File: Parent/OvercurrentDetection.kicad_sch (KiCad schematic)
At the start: 2 parts, among them U62 INA138

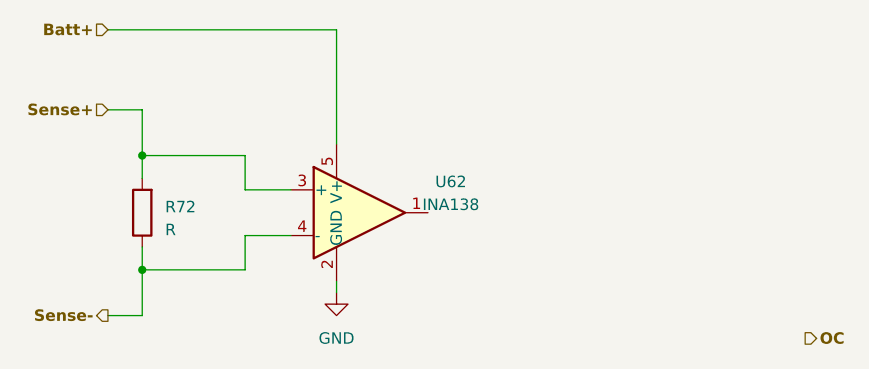
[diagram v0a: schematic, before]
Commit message: Updated Parent - Moved workspace to cloud
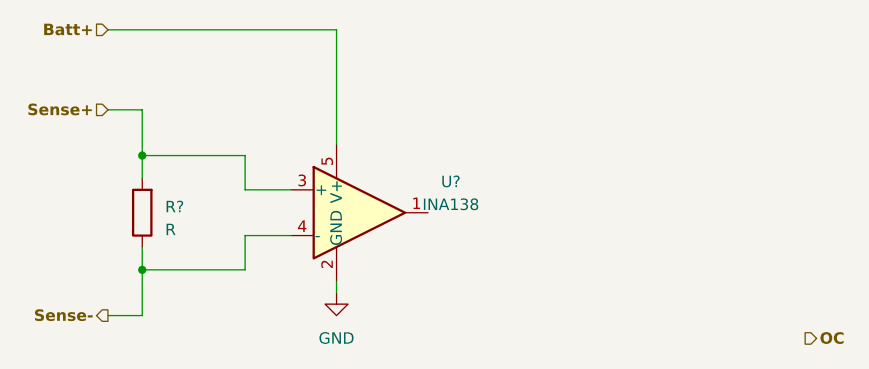
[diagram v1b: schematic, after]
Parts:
- renumbered R72 to R?, U62 to U?
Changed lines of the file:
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@@
   (symbol (lib_id "Amplifier_Current:INA138") (at 149.86 85.09 0) (unit 1)
     (in_bom yes) (on_board yes) (dnp no) (fields_autoplaced)
-    (property "Reference" "U62" (at 160.02 81.6611 0)
+    (property "Reference" "U?" (at 160.02 81.6611 0)
       (effects (font (size 1.27 1.27)))
     )
@@
       (project "Parent"
         (path "/1451ec1d-c665-471b-ba41-1d89ef6a63bf/687e81f5-5c64-42d1-9826-1f675bc9cd55"
-          (reference "U62") (unit 1)
+          (reference "U?") (unit 1)
         )
       )
@@
   (symbol (lib_id "power:GND") (at 147.32 93.98 0) (unit 1)
     (in_bom yes) (on_board yes) (dnp no) (fields_autoplaced)
-    (property "Reference" "#PWR029" (at 147.32 100.33 0)
+    (property "Reference" "#PWR?" (at 147.32 100.33 0)
       (effects (font (size 1.27 1.27)) hide)
     )
@@
       (project "Parent"
         (path "/1451ec1d-c665-471b-ba41-1d89ef6a63bf/687e81f5-5c64-42d1-9826-1f675bc9cd55"
-          (reference "#PWR029") (unit 1)
+          (reference "#PWR?") (unit 1)
         )
       )
@@
   (symbol (lib_id "Device:R") (at 125.73 85.09 180) (unit 1)
     (in_bom yes) (on_board yes) (dnp no) (fields_autoplaced)
-    (property "Reference" "R72" (at 128.27 84.455 0)
+    (property "Reference" "R?" (at 128.27 84.455 0)
       (effects (font (size 1.27 1.27)) (justify right))
     )
@@
       (project "Parent"
         (path "/1451ec1d-c665-471b-ba41-1d89ef6a63bf/687e81f5-5c64-42d1-9826-1f675bc9cd55"
-          (reference "R72") (unit 1)
+          (reference "R?") (unit 1)
         )
       )
